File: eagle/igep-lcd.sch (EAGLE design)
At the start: 9 parts, among them IC1 LM1117IMPX-3.3, U1 SN74LVC8T245PW, U2 SN74LVC8T245PW, U3 SN74LVC8T245PW, U4 SN74LVC8T245PW

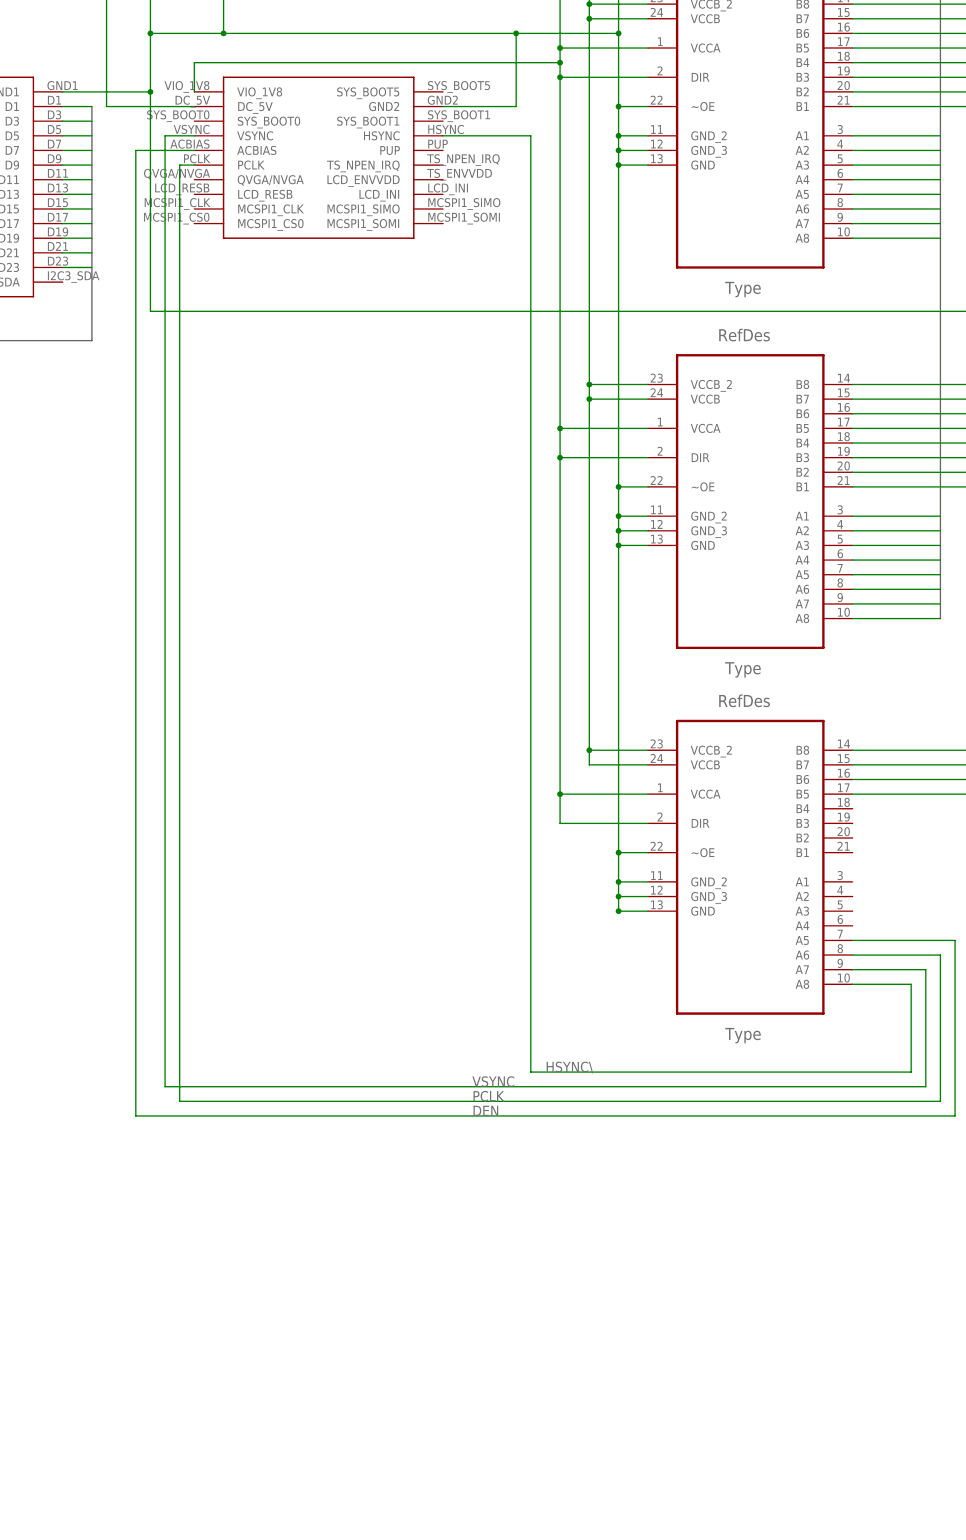
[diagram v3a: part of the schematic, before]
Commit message: Added LCD backlight driver (lacking the connector)
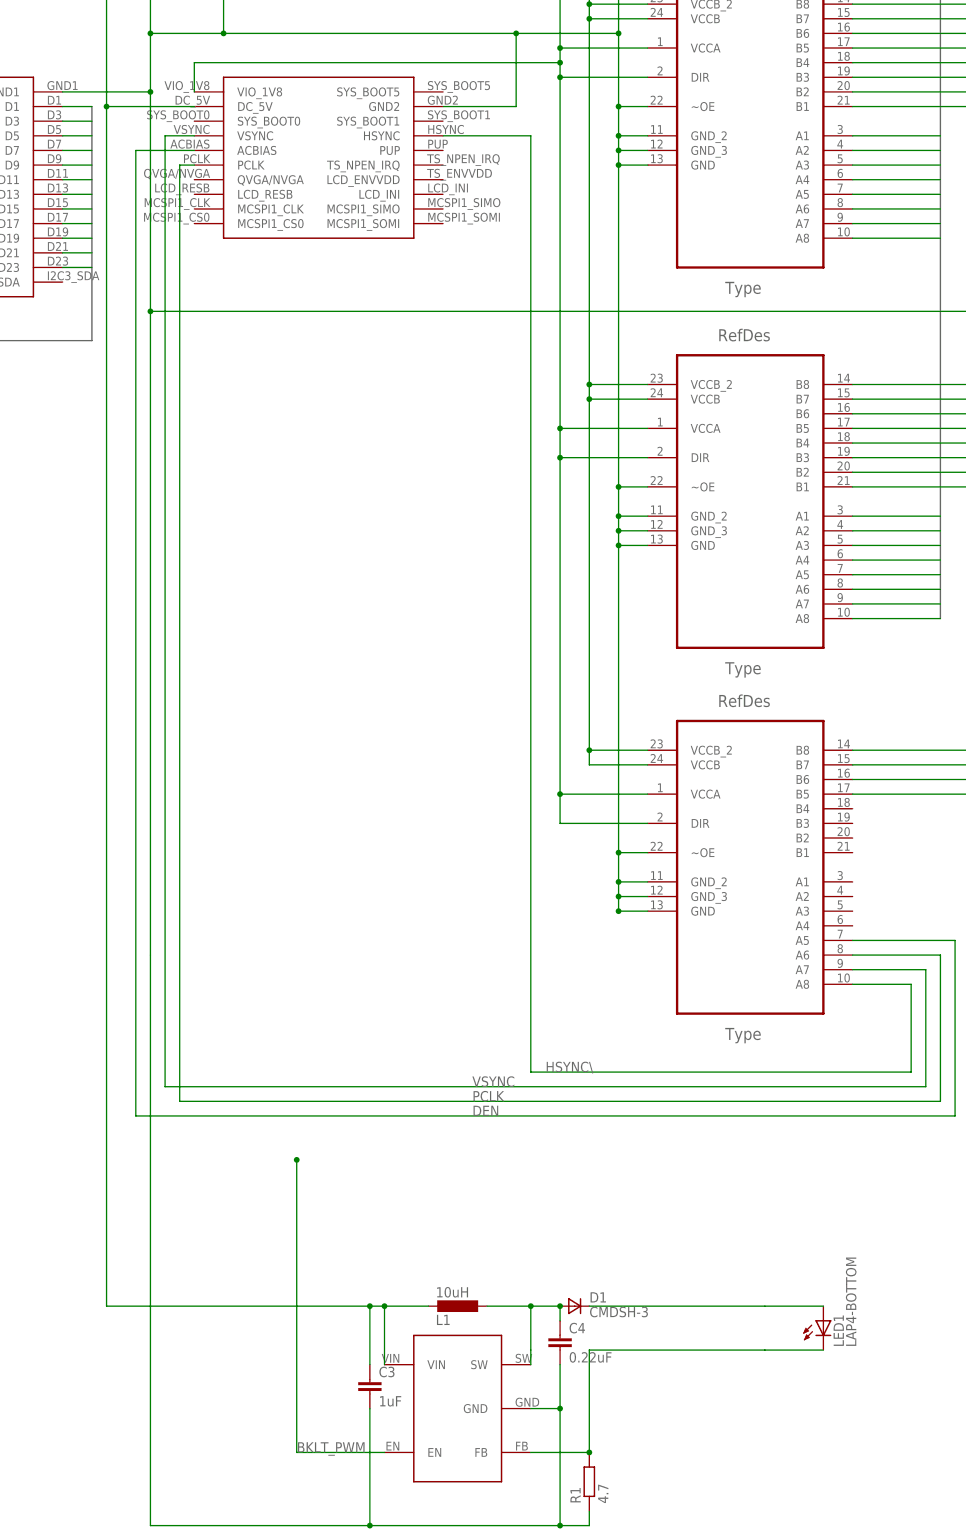
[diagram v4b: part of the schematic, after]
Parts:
- added C3: 1uF, resistor:C-EU025-024X044
- added C4: 0.22uF, resistor:C-EU025-024X044
- added D1: CMDSH-3, zetex:DSOD323
- added L1: 10uH, resistor:L-EU0204/5
- added LED1: LAP4-BOTTOM, led:LAP4-BOTTOM
- added R1: 4.7, resistor:R-EU_0204/2V
- added U$2: MIC2287, mic2287:MIC2287
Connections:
- new net BKLT_PWM: U$2.EN
- new net N$13: D1.C, LED1.A
- new net N$14: LED1.C, R1.2, U$2.FB
- new net N$8: C4.1, D1.A, L1.1, U$2.SW
- net N$1: now also C3.1, L1.2, U$2.VIN
- net N$2: now also C3.2, C4.2, R1.1, U$2.GND
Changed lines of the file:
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@@
 <part name="C1" library="capacitor-wima" deviceset="C" device="2,5-3" value="22uF"/>
 <part name="C2" library="capacitor-wima" deviceset="C" device="2,5-3" value="10uF"/>
+<part name="U$2" library="mic2287" deviceset="MIC2287" device=""/>
+<part name="C3" library="resistor" deviceset="C-EU" device="025-024X044" value="1uF"/>
+<part name="L1" library="resistor" deviceset="L-EU" device="0204/5" value="10uH"/>
+<part name="D1" library="zetex" deviceset="D" device="SOD323" value="CMDSH-3"/>
+<part name="C4" library="resistor" deviceset="C-EU" device="025-024X044" value="0.22uF"/>
+<part name="R1" library="resistor" deviceset="R-EU_" device="0204/2V" value="4.7"/>
+<part name="LED1" library="led" deviceset="*P4" device="-BOTTOM" technology="LA"/>
 </parts>
 <sheets>
@@
 <instance part="C1" gate="G$1" x="66.04" y="71.12"/>
 <instance part="C2" gate="G$1" x="48.26" y="71.12"/>
+<instance part="U$2" gate="G$1" x="106.68" y="-180.34" rot="MR90"/>
+<instance part="C3" gate="G$1" x="91.44" y="-175.26"/>
+<instance part="L1" gate="G$1" x="106.68" y="-162.56" rot="MR90"/>
+<instance part="D1" gate="G$1" x="127" y="-162.56"/>
+<instance part="C4" gate="G$1" x="124.46" y="-167.64"/>
+<instance part="R1" gate="G$1" x="129.54" y="-193.04" rot="R90"/>
+<instance part="LED1" gate="G$1" x="170.18" y="-165.1"/>
 </instances>
 <busses>
@@
 <wire x1="48.26" y1="73.66" x2="45.72" y2="73.66" width="0.1524" layer="91"/>
 <junction x="45.72" y="73.66"/>
+<wire x1="45.72" y1="45.72" x2="45.72" y2="-162.56" width="0.1524" layer="91"/>
+<pinref part="C3" gate="G$1" pin="1"/>
+<wire x1="91.44" y1="-172.72" x2="91.44" y2="-162.56" width="0.1524" layer="91"/>
+<wire x1="91.44" y1="-162.56" x2="93.98" y2="-162.56" width="0.1524" layer="91"/>
+<pinref part="U$2" gate="G$1" pin="VIN"/>
+<pinref part="L1" gate="G$1" pin="2"/>
+<wire x1="93.98" y1="-162.56" x2="93.98" y2="-172.72" width="0.1524" layer="91"/>
+<wire x1="101.6" y1="-162.56" x2="93.98" y2="-162.56" width="0.1524" layer="91"/>
+<junction x="93.98" y="-162.56"/>
+<wire x1="45.72" y1="-162.56" x2="91.44" y2="-162.56" width="0.1524" layer="91"/>
+<junction x="91.44" y="-162.56"/>
+<junction x="45.72" y="45.72"/>
 </segment>
 </net>
@@
 <wire x1="139.7" y1="99.06" x2="134.62" y2="99.06" width="0.1524" layer="91"/>
 <junction x="134.62" y="99.06"/>
+<wire x1="53.34" y1="10.16" x2="53.34" y2="-101.6" width="0.1524" layer="91"/>
+<wire x1="53.34" y1="-101.6" x2="53.34" y2="-200.66" width="0.1524" layer="91"/>
+<pinref part="U$2" gate="G$1" pin="GND"/>
+<wire x1="119.38" y1="-180.34" x2="124.46" y2="-180.34" width="0.1524" layer="91"/>
+<wire x1="124.46" y1="-180.34" x2="124.46" y2="-200.66" width="0.1524" layer="91"/>
+<pinref part="C3" gate="G$1" pin="2"/>
+<wire x1="124.46" y1="-200.66" x2="91.44" y2="-200.66" width="0.1524" layer="91"/>
+<wire x1="91.44" y1="-200.66" x2="91.44" y2="-180.34" width="0.1524" layer="91"/>
+<pinref part="C4" gate="G$1" pin="2"/>
+<wire x1="124.46" y1="-172.72" x2="124.46" y2="-180.34" width="0.1524" layer="91"/>
+<junction x="124.46" y="-180.34"/>
+<pinref part="R1" gate="G$1" pin="1"/>
+<wire x1="124.46" y1="-200.66" x2="129.54" y2="-200.66" width="0.1524" layer="91"/>
+<wire x1="129.54" y1="-200.66" x2="129.54" y2="-198.12" width="0.1524" layer="91"/>
+<junction x="124.46" y="-200.66"/>
+<wire x1="53.34" y1="-200.66" x2="91.44" y2="-200.66" width="0.1524" layer="91"/>
+<junction x="53.34" y="10.16"/>
+<junction x="91.44" y="-200.66"/>
 </segment>
 </net>
@@
 </segment>
 </net>
+<net name="N$8" class="0">
+<segment>
+<pinref part="L1" gate="G$1" pin="1"/>
+<wire x1="111.76" y1="-162.56" x2="119.38" y2="-162.56" width="0.1524" layer="91"/>
+<wire x1="119.38" y1="-162.56" x2="119.38" y2="-170.18" width="0.1524" layer="91"/>
+<pinref part="U$2" gate="G$1" pin="SW"/>
+<wire x1="119.38" y1="-170.18" x2="119.38" y2="-172.72" width="0.1524" layer="91"/>
+<pinref part="C4" gate="G$1" pin="1"/>
+<wire x1="124.46" y1="-165.1" x2="124.46" y2="-162.56" width="0.1524" layer="91"/>
+<wire x1="124.46" y1="-162.56" x2="119.38" y2="-162.56" width="0.1524" layer="91"/>
+<junction x="119.38" y="-162.56"/>
+<pinref part="D1" gate="G$1" pin="A"/>
+<junction x="124.46" y="-162.56"/>
+</segment>
+</net>
+<net name="N$13" class="0">
+<segment>
+<pinref part="D1" gate="G$1" pin="C"/>
+<wire x1="129.54" y1="-162.56" x2="160.02" y2="-162.56" width="0.1524" layer="91"/>
+<pinref part="LED1" gate="G$1" pin="A"/>
+<wire x1="160.02" y1="-162.56" x2="170.18" y2="-162.56" width="0.1524" layer="91"/>
+</segment>
+</net>
+<net name="N$14" class="0">
+<segment>
+<wire x1="160.02" y1="-170.18" x2="129.54" y2="-170.18" width="0.1524" layer="91"/>
+<wire x1="129.54" y1="-170.18" x2="129.54" y2="-187.96" width="0.1524" layer="91"/>
+<pinref part="U$2" gate="G$1" pin="FB"/>
+<wire x1="129.54" y1="-187.96" x2="119.38" y2="-187.96" width="0.1524" layer="91"/>
+<pinref part="R1" gate="G$1" pin="2"/>
+<junction x="129.54" y="-187.96"/>
+<pinref part="LED1" gate="G$1" pin="C"/>
+<wire x1="170.18" y1="-170.18" x2="160.02" y2="-170.18" width="0.1524" layer="91"/>
+</segment>
+</net>
+<net name="BKLT_PWM" class="0">
+<segment>
+<pinref part="U$2" gate="G$1" pin="EN"/>
+<wire x1="93.98" y1="-187.96" x2="78.74" y2="-187.96" width="0.1524" layer="91"/>
+<wire x1="78.74" y1="-187.96" x2="78.74" y2="-137.16" width="0.1524" layer="91"/>
+<label x="78.74" y="-187.96" size="1.778" layer="95"/>
+<junction x="78.74" y="-137.16"/>
+</segment>
+</net>

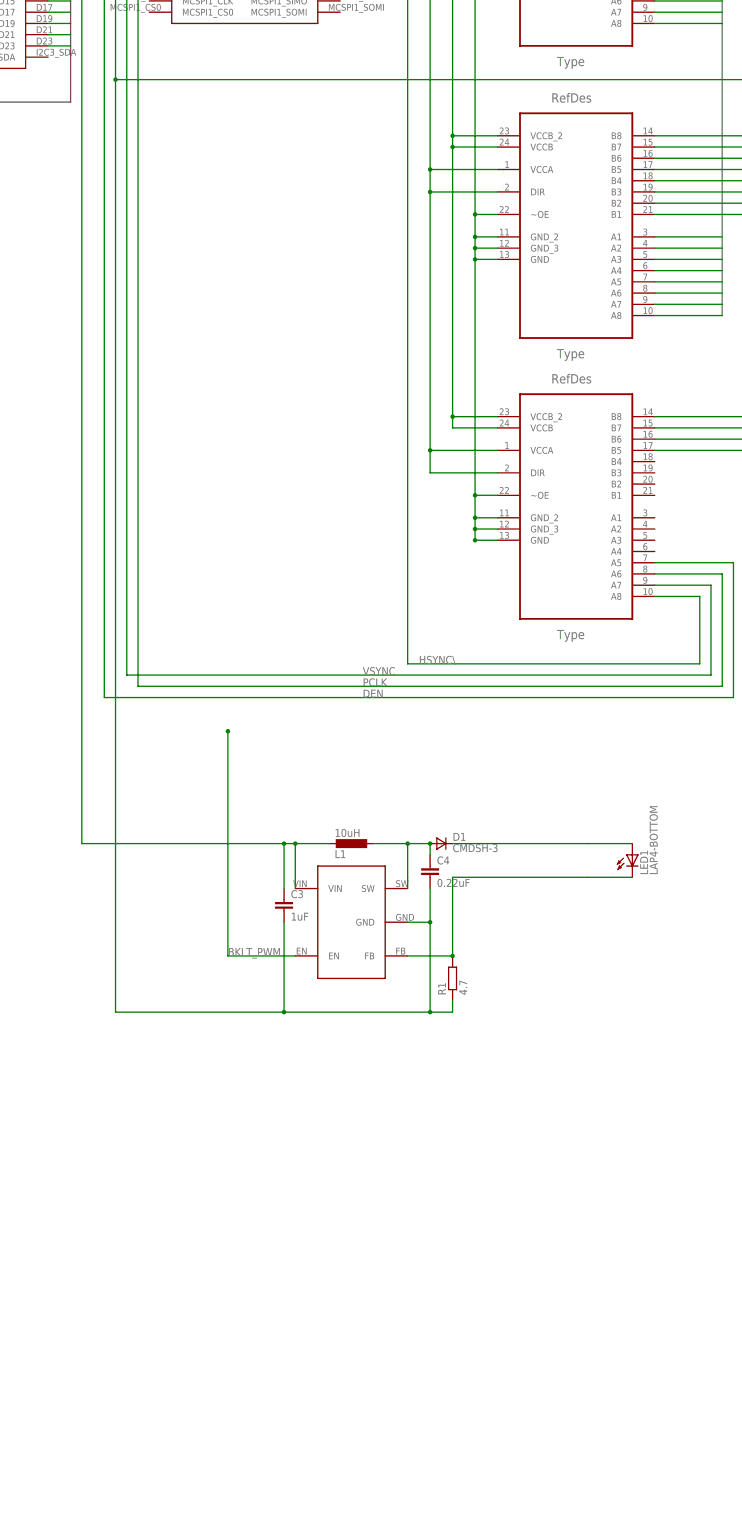
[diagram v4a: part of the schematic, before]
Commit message: Added all backlight controllers.
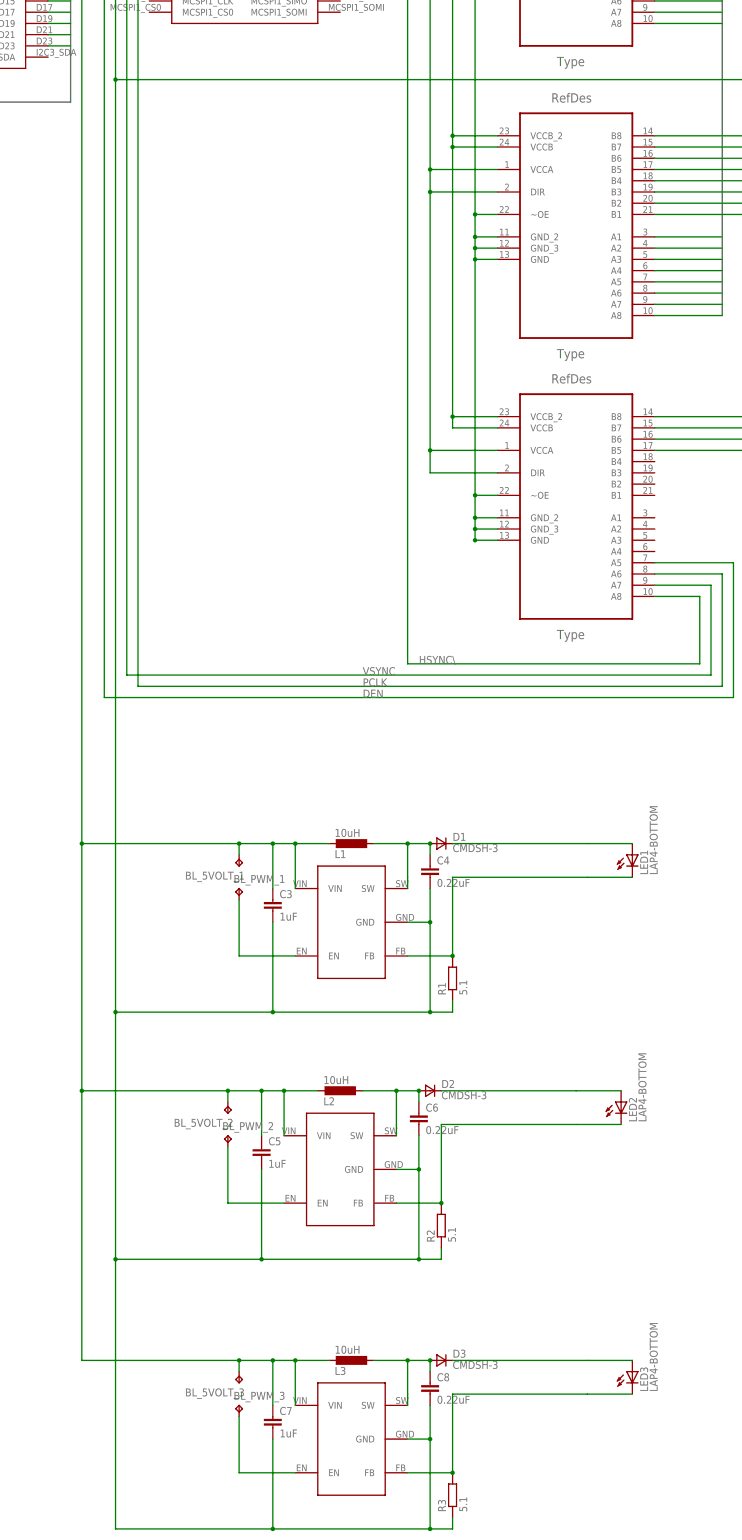
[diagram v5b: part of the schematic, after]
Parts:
- added BL_5VOLT_1, BL_5VOLT_2, BL_5VOLT_3, BL_PWM_1, BL_PWM_2, BL_PWM_3: TPB1,27, testpad:TPB1,27
- added C5, C7: 1uF, resistor:C-EU025-024X044
- added C6, C8: 0.22uF, resistor:C-EU025-024X044
- added D2, D3: CMDSH-3, zetex:DSOD323
- added L2, L3: 10uH, resistor:L-EU0204/5
- added LED2, LED3: LAP4-BOTTOM, led:LAP4-BOTTOM
- added R2, R3: 5.1, resistor:R-EU_0204/2V
- added U$3, U$4: MIC2287, mic2287:MIC2287
- R1: value 4.7 -> 5.1
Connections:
- removed net BKLT_PWM: U$2.EN
- removed net N$1: C2.1, C3.1, IC1.IN, L1.2, U$1.DC_5V, U$2.VIN
- removed net N$2: C1.2, C2.2, C3.2, C4.2, IC1.GND, LCD-1.1, LCD-2.1, LCD-29.1, LCD-37.1, LCD-38.1, R1.1, U$1.GND1, U$1.GND2, U$2.GND, U1.GND, U1.GND_2, U1.GND_3, U1.~OE, U2.GND, U2.GND_2, U2.GND_3, U2.~OE, U3.GND, U3.GND_2, U3.GND_3, U3.~OE, U4.GND, U4.GND_2, U4.GND_3, U4.~OE
- new net N$12: C1.2, C2.2, C3.2, C4.2, C5.2, C6.2, C7.2, C8.2, IC1.GND, LCD-1.1, LCD-2.1, LCD-29.1, LCD-37.1, LCD-38.1, R1.1, R2.1, R3.1, U$1.GND1, U$1.GND2, U$2.GND, U$3.GND, U$4.GND, U1.GND, U1.GND_2, U1.GND_3, U1.~OE, U2.GND, U2.GND_2, U2.GND_3, U2.~OE, U3.GND, U3.GND_2, U3.GND_3, U3.~OE, U4.GND, U4.GND_2, U4.GND_3, U4.~OE
- new net N$15: C6.1, D2.A, L2.1, U$3.SW
- new net N$16: D2.C, LED2.A
- new net N$17: LED2.C, R2.2, U$3.FB
- new net N$18: BL_PWM_2.TP, U$3.EN
- new net N$19: BL_5VOLT_1.TP, BL_5VOLT_2.TP, BL_5VOLT_3.TP, C2.1, C3.1, C5.1, C7.1, IC1.IN, L1.2, L2.2, L3.2, U$1.DC_5V, U$2.VIN, U$3.VIN, U$4.VIN
- new net N$21: C8.1, D3.A, L3.1, U$4.SW
- new net N$22: D3.C, LED3.A
- new net N$23: LED3.C, R3.2, U$4.FB
- new net N$24: BL_PWM_3.TP, U$4.EN
- new net N$6: BL_PWM_1.TP, U$2.EN
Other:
- moved on the sheet: C3
